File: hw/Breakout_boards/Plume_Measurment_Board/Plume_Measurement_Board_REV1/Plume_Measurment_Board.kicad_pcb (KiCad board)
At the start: 2 copper layers, 25 parts, among them J2 Conn_01x04, J4 Conn_01x04, U2 LMP7721MA/NOPB, U3 LMP2022MA/NOPB, U6 TPS62153, U7 AD7176-2BRUZ

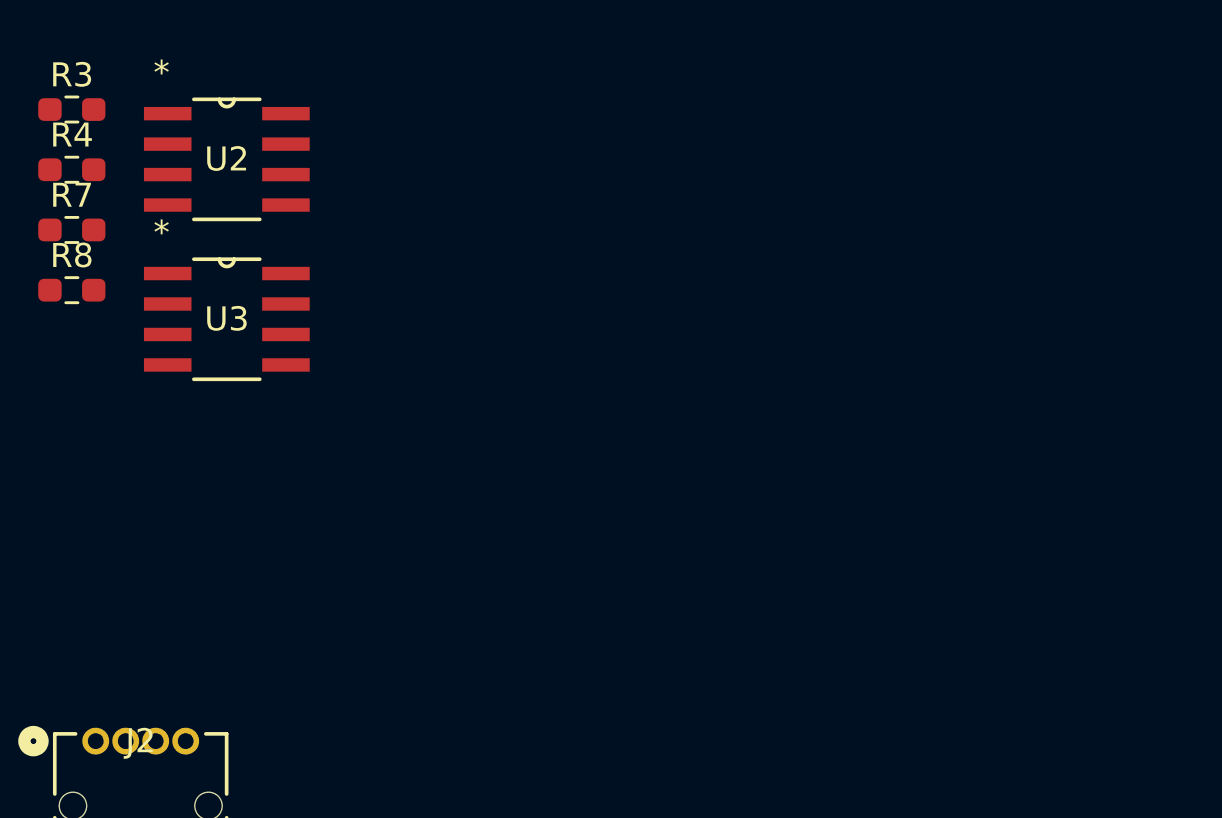
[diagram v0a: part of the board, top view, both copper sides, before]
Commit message: AD8475 Buffer Footprint Addition
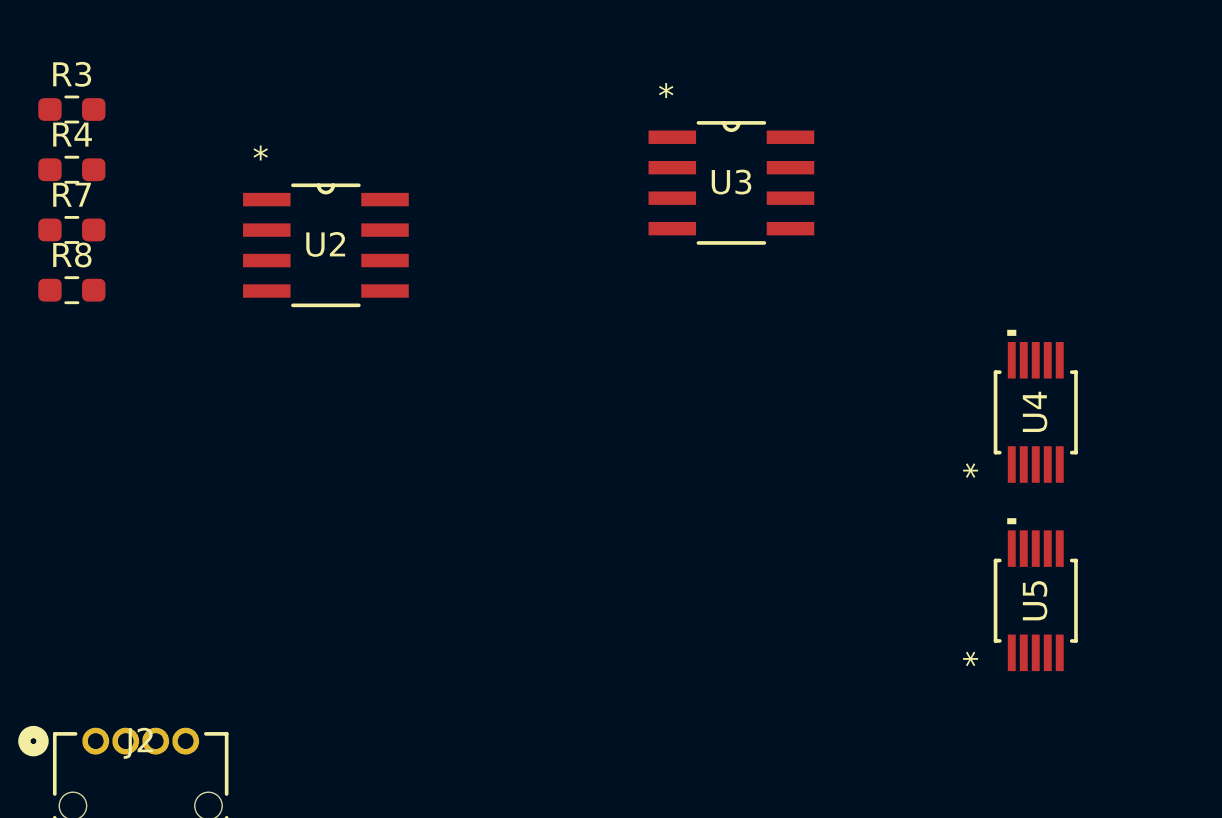
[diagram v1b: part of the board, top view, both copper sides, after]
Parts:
- added U4: AD8475ARMZ, Buffer_Analog_Devices:RM_10_ADI, F.Cu at (103.3, 44.6)
- added U5: AD8475ARMZ, Buffer_Analog_Devices:RM_10_ADI, F.Cu at (103.3, 52.4)
- moved U3 21.8 mm to (90.6, 35.0)
- moved U2 5.47 mm to (73.7, 37.6)

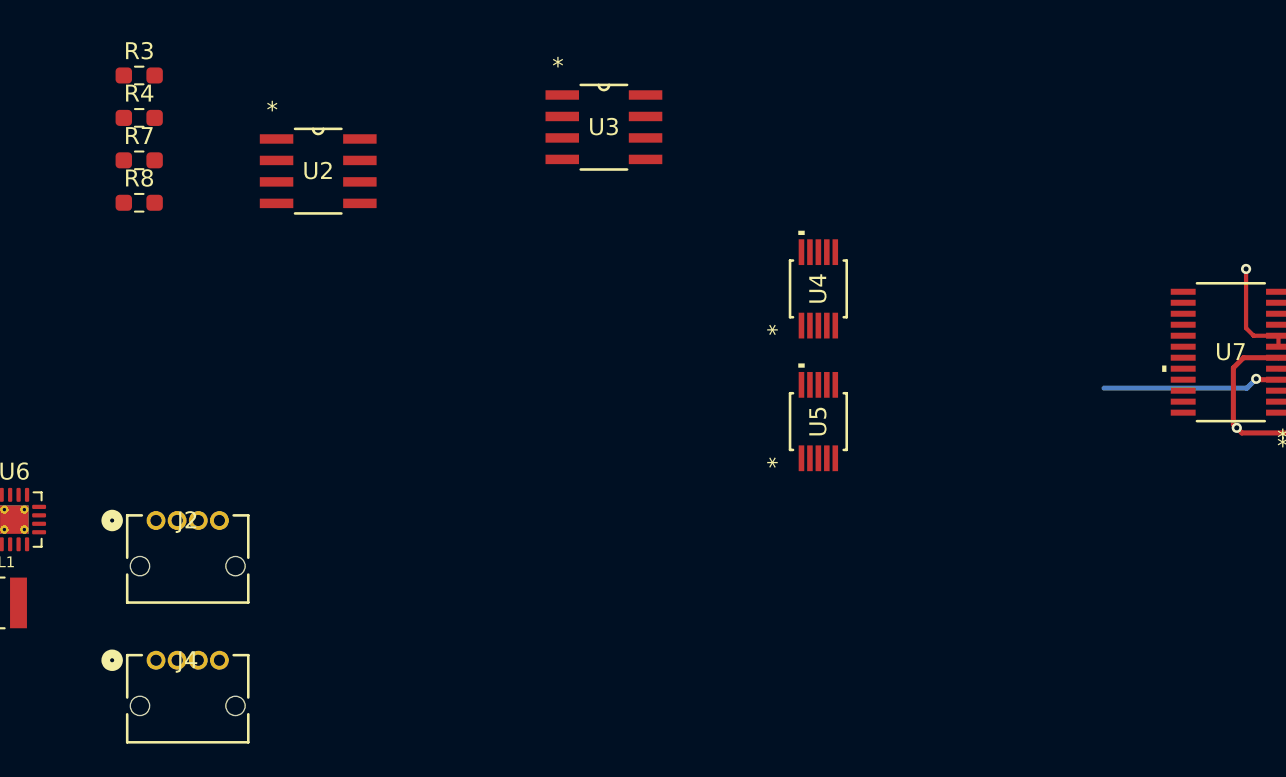
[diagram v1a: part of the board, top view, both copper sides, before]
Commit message: Schematic Progress Buffer/2nd Stage Amplifier Integration
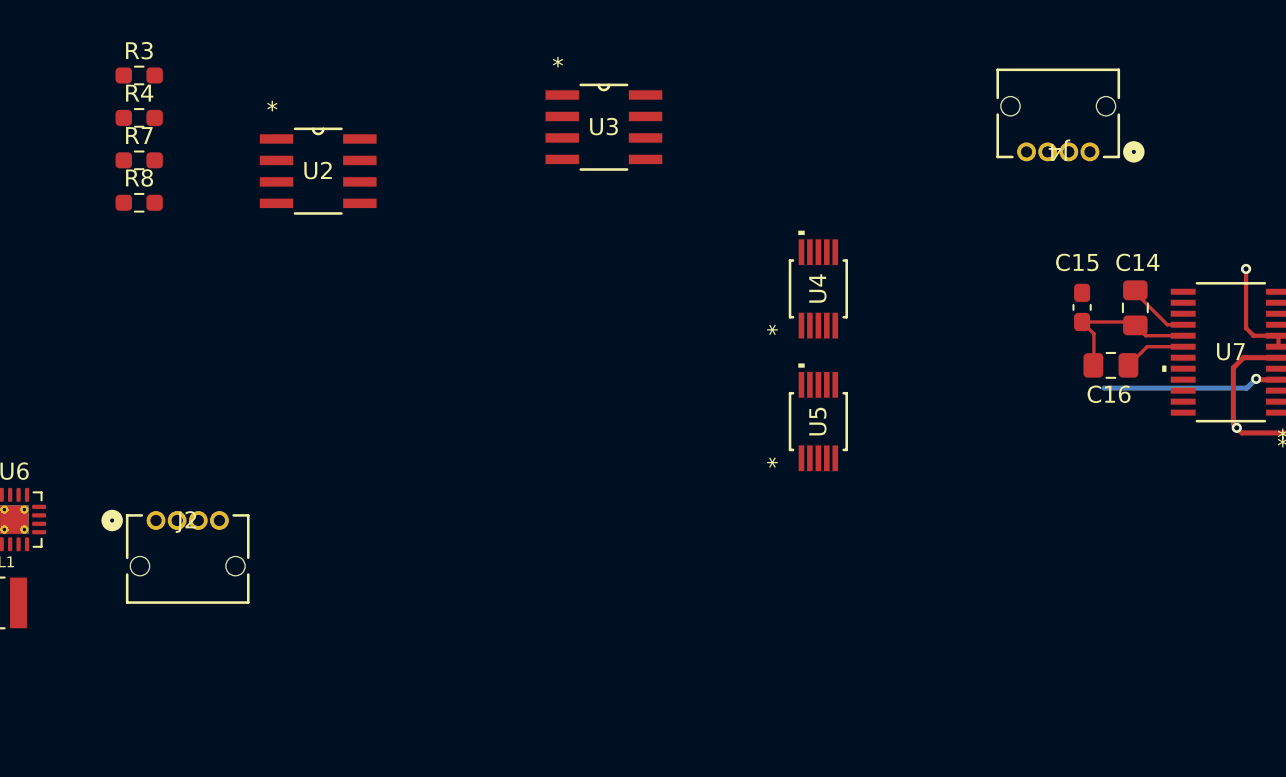
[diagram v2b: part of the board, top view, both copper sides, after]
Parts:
- added C14: 10uF, Capacitor_SMD:C_0805_2012Metric_Pad1.18x1.45mm_HandSolder, F.Cu at (122.0, 45.7)
- added C15: 100nF, Capacitor_SMD:C_0603_1608Metric_Pad1.08x0.95mm_HandSolder, F.Cu at (118.8, 45.7)
- added C16: 1uF, Capacitor_SMD:C_0805_2012Metric_Pad1.18x1.45mm_HandSolder, F.Cu at (120.6, 49.1)
- moved J4 62.9 mm to (119.3, 36.5), turned to 180 degrees
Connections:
- C11 pad 2: /VSS -> GND
- C12 pad 1: /VSS -> GND
- C13 pad 1: /VSS -> GND
- C4 pad 2: /VSS -> GND
- U7 pad 16: unconnected-(U7-IOVDD-Pad16) -> +3V3
- U7 pad 17: unconnected-(U7-DGND-Pad17) -> GND
- U7 pad 18: unconnected-(U7-REGCAPD-Pad18) -> Net-(U7-REGCAPD)
- U7 pad 6: /VSS -> GND
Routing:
- net GND: track 0.00 -> 33.5 mm, vias 0 -> 1
- net /VSS: track 24.3 -> 0.00 mm, vias 1 -> 0
- net +3V3: track 0.00 -> 3.76 mm
- net Net-(U7-REGCAPD): track 0.00 -> 3.70 mm

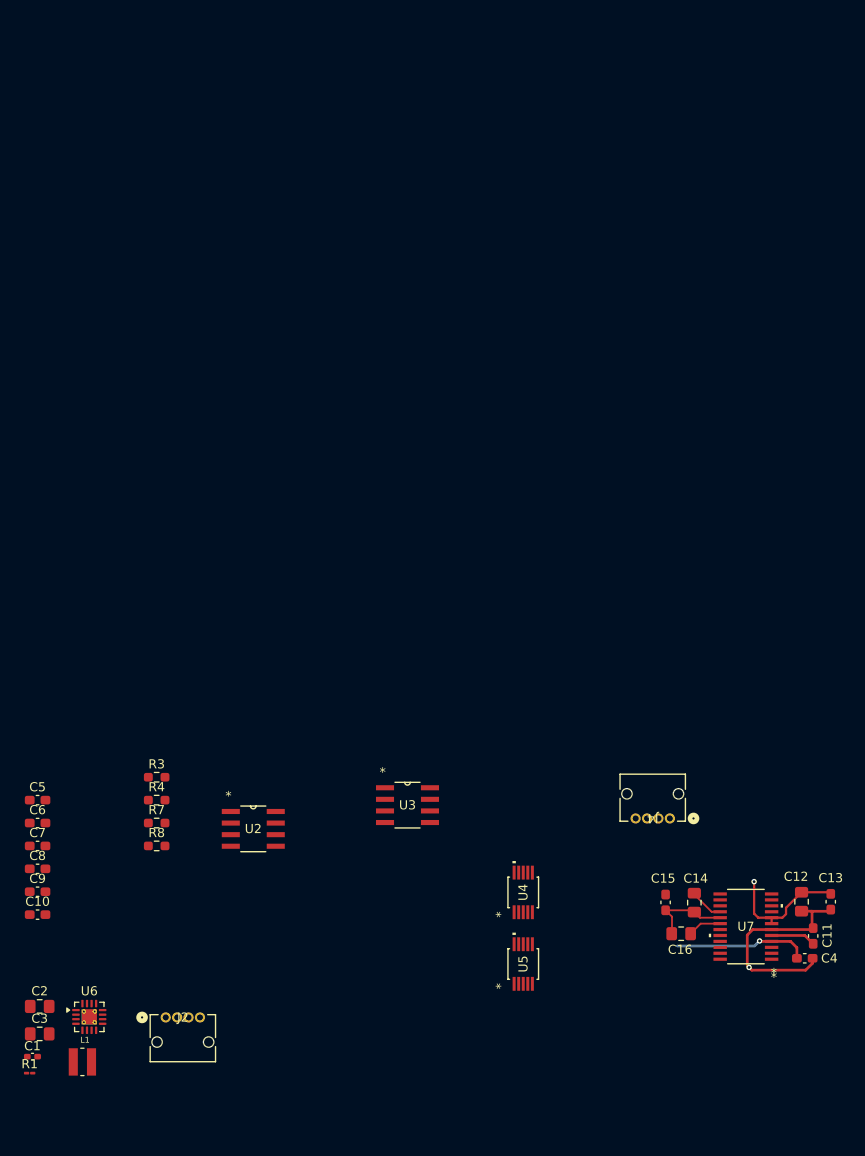
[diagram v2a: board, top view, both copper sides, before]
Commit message: Progress Routing Buffer Chips
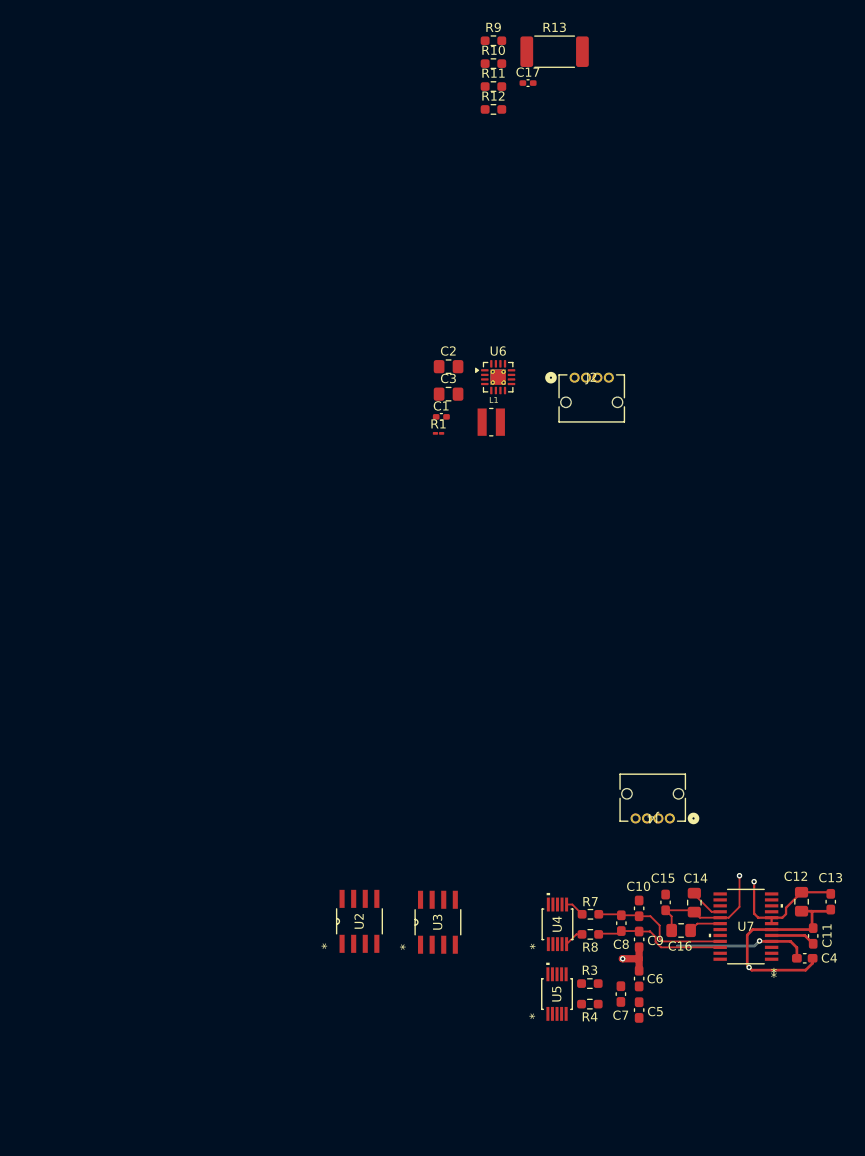
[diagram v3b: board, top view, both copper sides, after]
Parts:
- added C17: .1pF, Capacitor_SMD:C_0402_1005Metric_Pad0.74x0.62mm_HandSolder, F.Cu at (103.8, -44.1)
- added R10: ?, Resistor_SMD:R_0603_1608Metric_Pad0.98x0.95mm_HandSolder, F.Cu at (100.0, -46.2)
- added R11: 1000, Resistor_SMD:R_0603_1608Metric_Pad0.98x0.95mm_HandSolder, F.Cu at (100.0, -43.7)
- added R12: 1000, Resistor_SMD:R_0603_1608Metric_Pad0.98x0.95mm_HandSolder, F.Cu at (100.0, -41.2)
- added R13: 1G, Resistor_SMD:R_2512_6332Metric_Pad1.40x3.35mm_HandSolder, F.Cu at (106.7, -47.6)
- added R9: ?, Resistor_SMD:R_0603_1608Metric_Pad0.98x0.95mm_HandSolder, F.Cu at (100.0, -48.8)
- moved C1 83.2 mm to (94.3, -7.54)
- moved L1 83.2 mm to (99.7, -6.96)
- moved R1 83.2 mm to (94.0, -5.73)
- moved U6 83.2 mm to (100.5, -11.9)
- moved C2 83.2 mm to (95.1, -13.0)
- moved C3 83.2 mm to (95.1, -10.0)
- moved J2 83.2 mm to (108.9, -11.8)
- moved C5 69.8 mm to (116.0, 57.5), turned to -90 degrees
- moved C6 68.1 mm to (116.0, 54.0), turned to -90 degrees
- moved C9 66.1 mm to (116.0, 49.7), turned to -90 degrees
- moved C7 66.0 mm to (114.0, 55.7), turned to 90 degrees
- moved C10 65.9 mm to (116.0, 46.3), turned to -90 degrees
- moved C8 64.3 mm to (114.0, 48.0), turned to 90 degrees
- moved R3 52.6 mm to (110.6, 54.6)
- moved R4 52.5 mm to (110.6, 56.8), turned to 180 degrees
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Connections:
- U2 pad 1: unconnected-(U2-IN+-Pad1) -> GND
- U2 pad 2: unconnected-(U2-NC-Pad2) -> /+2.5V
- U2 pad 3: unconnected-(U2-V--Pad3) -> GND
- U2 pad 4: unconnected-(U2-OUT-Pad4) -> /Amplified_Plume_1
- U2 pad 6: unconnected-(U2-V+-Pad6) -> +5V
- U2 pad 7: unconnected-(U2-NC-Pad7) -> /+2.5V
- U2 pad 8: unconnected-(U2-IN--Pad8) -> /Plume
- U3 pad 1: unconnected-(U3A-OUTA-Pad1) -> /1_IN0.8+
- U3 pad 2: unconnected-(U3A-INA--Pad2) -> Net-(U3A-INA-)
- U3 pad 3: unconnected-(U3A-INA+-Pad3) -> /+2.5V
- U3 pad 4: unconnected-(U3A-V--Pad4) -> GND
- U3 pad 5: unconnected-(U3A-INB+-Pad5) -> /+2.5V
- U3 pad 6: unconnected-(U3A-INB--Pad6) -> Net-(U3A-INB-)
- U3 pad 7: unconnected-(U3A-OUTB-Pad7) -> /2_IN0.8+
- U3 pad 8: unconnected-(U3A-V+-Pad8) -> +5V
- U4 pad 1: unconnected-(U4-IN0.8X--Pad1) -> /+2.5V
- U4 pad 10: unconnected-(U4-IN0.8X+-Pad10) -> /1_IN0.8+
- U4 pad 3: unconnected-(U4-VS+-Pad3) -> +5V
- U4 pad 8: unconnected-(U4-VS--Pad8) -> GND
- U5 pad 1: unconnected-(U5-IN0.8X--Pad1) -> /+2.5V
- U5 pad 10: unconnected-(U5-IN0.8X+-Pad10) -> /2_IN0.8+
- U5 pad 3: unconnected-(U5-VS+-Pad3) -> +5V
- U5 pad 8: unconnected-(U5-VS--Pad8) -> GND
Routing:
- net Net-(U7-AIN0): track 0.00 -> 15.4 mm
- net Net-(U7-AIN1): track 0.00 -> 14.5 mm
- net GND: track 33.5 -> 43.9 mm, vias 1 -> 3
- net /-OUT_1: track 0.00 -> 2.14 mm
- net /+OUT_1: track 0.00 -> 2.13 mm

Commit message: Good Routing Progress
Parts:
- added C18: 1uF, Capacitor_SMD:C_0805_2012Metric_Pad1.18x1.45mm_HandSolder, B.Cu at (108.7, 51.9)
- added C19: 1uF, Capacitor_SMD:C_0603_1608Metric_Pad1.08x0.95mm_HandSolder, B.Cu at (105.0, 51.8)
- added C20: 1uF, Capacitor_SMD:C_0603_1608Metric_Pad1.08x0.95mm_HandSolder, B.Cu at (105.8, 63.5)
- added C21: 1uF, Capacitor_SMD:C_0805_2012Metric_Pad1.18x1.45mm_HandSolder, B.Cu at (110.4, 63.7)
- added C22: 1uF, Capacitor_SMD:C_0603_1608Metric_Pad1.08x0.95mm_HandSolder, B.Cu at (102.0, 49.4)
- added C23: 1uF, Capacitor_SMD:C_0805_2012Metric_Pad1.18x1.45mm_HandSolder, B.Cu at (110.4, 66.7)
- moved U3 5.76 mm to (98.0, 51.9)
- moved U2 5.59 mm to (89.2, 51.8)
- moved C7 0.27 mm to (114.0, 55.5)
- turned R3 to 180 degrees
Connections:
- C10 pad 1: GND -> /+2.5V
- C5 pad 2: GND -> /+2.5V
- C6 pad 1: GND -> /+2.5V
- C9 pad 2: GND -> /+2.5V
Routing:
- net GND: track 43.9 -> 79.1 mm, vias 3 -> 4
- net /+2.5V: track 14.8 -> 46.6 mm, vias 1 -> 4
- net +5V: track 14.4 -> 32.5 mm, vias 1 -> 3
- net Net-(U7-AIN3): track 0.00 -> 17.3 mm
- net Net-(U7-AIN2): track 0.00 -> 16.2 mm
- net /+OUT_2: track 0.00 -> 2.13 mm
- net /-OUT_2: track 0.00 -> 2.11 mm
